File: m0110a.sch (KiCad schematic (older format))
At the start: 177 parts

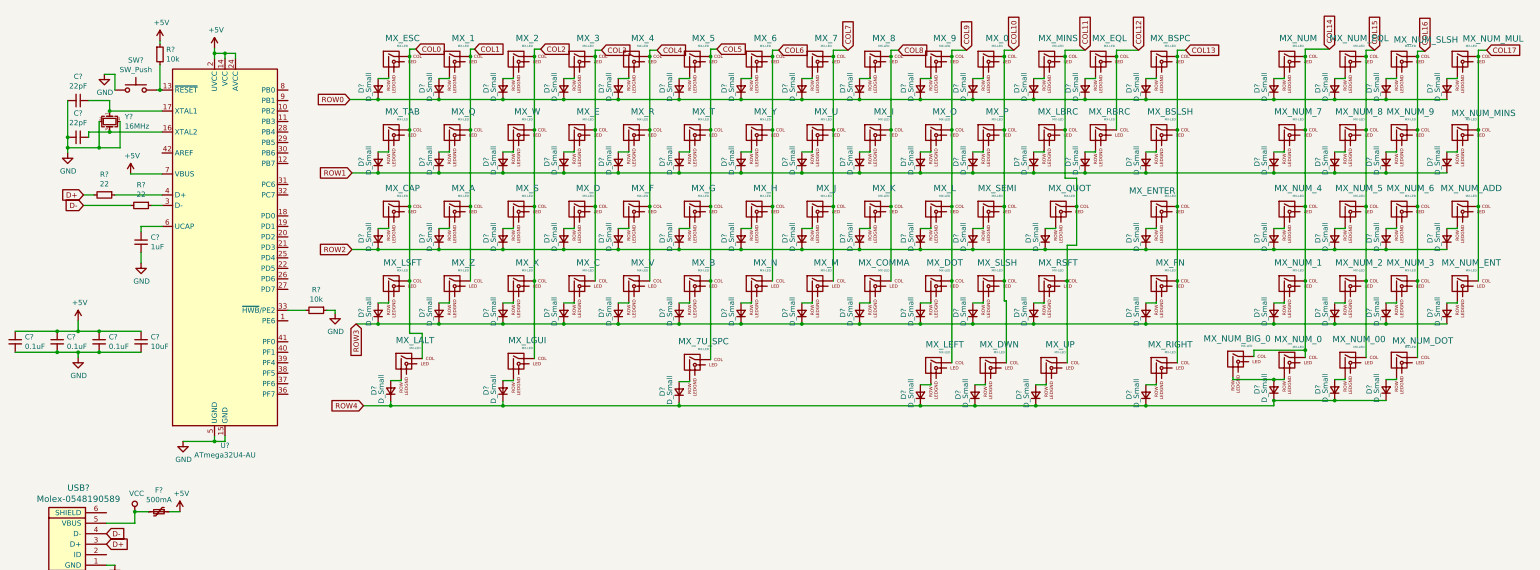
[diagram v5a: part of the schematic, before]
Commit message: Add footprint associations
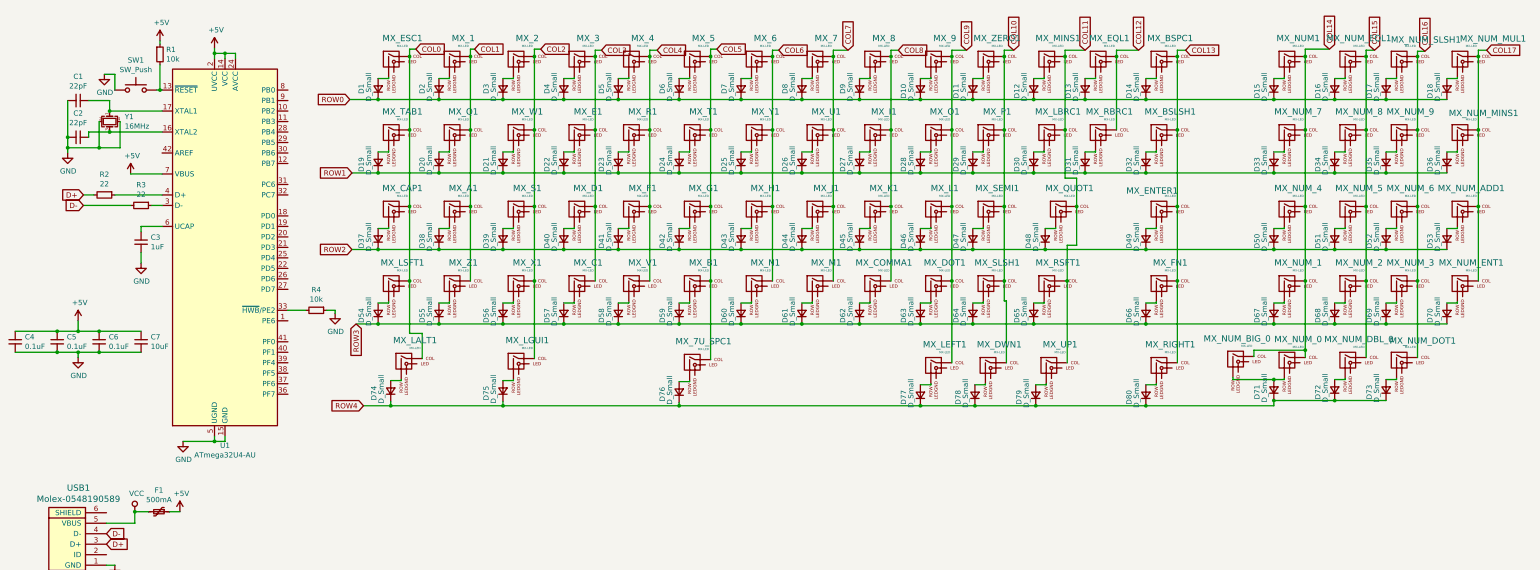
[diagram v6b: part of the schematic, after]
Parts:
- C1, C2, C3, C4, C5, C6, C7: renamed from C?; footprint (none) -> Capacitor_SMD:C_0805_2012Metric
- D1, D10, D11, D12, D13, D14, D15, D16, D17, D18, D19, D2, D20, D21, D22, D23, D24, D25, D26, D27, D28, D29, D3, D30, D31, D32, D33, D34, D35, D36, D37, D38, D39, D4, D40, D41, D42, D43, D44, D45, D46, D47, D48, D49, D5, D50, D51, D52, D53, D54, D55, D56, D57, D58, D59, D6, D60, D61, D62, D63, D64, D65, D66, D67, D68, D69, D7, D70, D71, D72, D73, D74, D75, D76, D77, D78, D79, D8, D80, D9: renamed from D?; footprint (none) -> Diode_SMD:D_SOD-123
- F1: renamed from F?; footprint (none) -> Fuse:Fuse_1206_3216Metric
- MX_1, MX_2, MX_3, MX_4, MX_5, MX_6, MX_7, MX_8, MX_9, MX_NUM_0, MX_NUM_1, MX_NUM_2, MX_NUM_3, MX_NUM_4, MX_NUM_5, MX_NUM_6, MX_NUM_7, MX_NUM_8, MX_NUM_9: footprint (none) -> MX_Alps_Hybrid:MX-1U
- MX_7U_SPC1: renamed from MX_7U_SPC; footprint (none) -> MX_Alps_Hybrid:MX-7U
- MX_A1: renamed from MX_A; footprint (none) -> MX_Alps_Hybrid:MX-1U
- MX_B1: renamed from MX_B; footprint (none) -> MX_Alps_Hybrid:MX-1U
- MX_BSLSH1: renamed from MX_BSLSH; footprint (none) -> MX_Alps_Hybrid:MX-1U
- MX_BSPC1: renamed from MX_BSPC; footprint (none) -> MX_Alps_Hybrid:MX-1.5U
- MX_C1: renamed from MX_C; footprint (none) -> MX_Alps_Hybrid:MX-1U
- MX_CAP1: renamed from MX_CAP; footprint (none) -> MX_Alps_Hybrid:MX-1.75U
- MX_COMMA1: renamed from MX_COMMA; footprint (none) -> MX_Alps_Hybrid:MX-1U
- MX_D1: renamed from MX_D; footprint (none) -> MX_Alps_Hybrid:MX-1U
- MX_DOT1: renamed from MX_DOT; footprint (none) -> MX_Alps_Hybrid:MX-1U
- MX_DWN1: renamed from MX_DWN; footprint (none) -> MX_Alps_Hybrid:MX-1U
- MX_E1: renamed from MX_E; footprint (none) -> MX_Alps_Hybrid:MX-1U
- MX_ENTER1: renamed from MX_ENTER; footprint (none) -> MX_Alps_Hybrid:MX-1.75U
- MX_EQL1: renamed from MX_EQL; footprint (none) -> MX_Alps_Hybrid:MX-1U
- MX_ESC1: renamed from MX_ESC; footprint (none) -> MX_Alps_Hybrid:MX-1U
- MX_F1: renamed from MX_F; footprint (none) -> MX_Alps_Hybrid:MX-1U
- MX_FN1: renamed from MX_FN; footprint (none) -> MX_Alps_Hybrid:MX-1U
- MX_G1: renamed from MX_G; footprint (none) -> MX_Alps_Hybrid:MX-1U
- MX_H1: renamed from MX_H; footprint (none) -> MX_Alps_Hybrid:MX-1U
- MX_I1: renamed from MX_I; footprint (none) -> MX_Alps_Hybrid:MX-1U
- MX_J1: renamed from MX_J; footprint (none) -> MX_Alps_Hybrid:MX-1U
- MX_K1: renamed from MX_K; footprint (none) -> MX_Alps_Hybrid:MX-1U
- MX_L1: renamed from MX_L; footprint (none) -> MX_Alps_Hybrid:MX-1U
- MX_LALT1: renamed from MX_LALT; footprint (none) -> MX_Alps_Hybrid:MX-1.5U
- MX_LBRC1: renamed from MX_LBRC; footprint (none) -> MX_Alps_Hybrid:MX-1U
- MX_LEFT1: renamed from MX_LEFT; footprint (none) -> MX_Alps_Hybrid:MX-1U
- MX_LGUI1: renamed from MX_LGUI; footprint (none) -> MX_Alps_Hybrid:MX-2U
- MX_LSFT1: renamed from MX_LSFT; footprint (none) -> MX_Alps_Hybrid:MX-2.25U
- MX_M1: renamed from MX_M; footprint (none) -> MX_Alps_Hybrid:MX-1U
- MX_MINS1: renamed from MX_MINS; footprint (none) -> MX_Alps_Hybrid:MX-1U
- MX_N1: renamed from MX_N; footprint (none) -> MX_Alps_Hybrid:MX-1U
- MX_NUM1: renamed from MX_NUM; footprint (none) -> MX_Alps_Hybrid:MX-1U
- MX_NUM_ADD1: renamed from MX_NUM_ADD; footprint (none) -> MX_Alps_Hybrid:MX-1U
- MX_NUM_BIG_0: footprint (none) -> MX_Alps_Hybrid:MX-2U
- MX_NUM_DBL_0: renamed from MX_NUM_00; footprint (none) -> MX_Alps_Hybrid:MX-1U
- MX_NUM_DOT1: renamed from MX_NUM_DOT; footprint (none) -> MX_Alps_Hybrid:MX-1U
- MX_NUM_ENT1: renamed from MX_NUM_ENT; footprint (none) -> MX_Alps_Hybrid:MX-2U
- MX_NUM_EQL1: renamed from MX_NUM_EQL; footprint (none) -> MX_Alps_Hybrid:MX-1U
- MX_NUM_MINS1: renamed from MX_NUM_MINS; footprint (none) -> MX_Alps_Hybrid:MX-1U
- MX_NUM_MUL1: renamed from MX_NUM_MUL; footprint (none) -> MX_Alps_Hybrid:MX-1U
- MX_NUM_SLSH1: renamed from MX_NUM_SLSH; footprint (none) -> MX_Alps_Hybrid:MX-1U
- MX_O1: renamed from MX_O; footprint (none) -> MX_Alps_Hybrid:MX-1U
- MX_P1: renamed from MX_P; footprint (none) -> MX_Alps_Hybrid:MX-1U
- MX_Q1: renamed from MX_Q; footprint (none) -> MX_Alps_Hybrid:MX-1U
- MX_QUOT1: renamed from MX_QUOT; footprint (none) -> MX_Alps_Hybrid:MX-1U
- MX_R1: renamed from MX_R; footprint (none) -> MX_Alps_Hybrid:MX-1U
- MX_RBRC1: renamed from MX_RBRC; footprint (none) -> MX_Alps_Hybrid:MX-1U
- MX_RIGHT1: renamed from MX_RIGHT; footprint (none) -> MX_Alps_Hybrid:MX-1U
- MX_RSFT1: renamed from MX_RSFT; footprint (none) -> MX_Alps_Hybrid:MX-1.25U
- MX_S1: renamed from MX_S; footprint (none) -> MX_Alps_Hybrid:MX-1U
- MX_SEMI1: renamed from MX_SEMI; footprint (none) -> MX_Alps_Hybrid:MX-1U
- MX_SLSH1: renamed from MX_SLSH; footprint (none) -> MX_Alps_Hybrid:MX-1U
- MX_T1: renamed from MX_T; footprint (none) -> MX_Alps_Hybrid:MX-1U
- MX_TAB1: renamed from MX_TAB; footprint (none) -> MX_Alps_Hybrid:MX-1.5U
- MX_U1: renamed from MX_U; footprint (none) -> MX_Alps_Hybrid:MX-1U
- MX_UP1: renamed from MX_UP; footprint (none) -> MX_Alps_Hybrid:MX-1U
- MX_V1: renamed from MX_V; footprint (none) -> MX_Alps_Hybrid:MX-1U
- MX_W1: renamed from MX_W; footprint (none) -> MX_Alps_Hybrid:MX-1U
- MX_X1: renamed from MX_X; footprint (none) -> MX_Alps_Hybrid:MX-1U
- MX_Y1: renamed from MX_Y; footprint (none) -> MX_Alps_Hybrid:MX-1U
- MX_Z1: renamed from MX_Z; footprint (none) -> MX_Alps_Hybrid:MX-1U
- MX_ZERO1: renamed from MX_0; footprint (none) -> MX_Alps_Hybrid:MX-1U
- R1, R2, R3, R4: renamed from R?; footprint (none) -> Resistor_SMD:R_0805_2012Metric
- SW1: renamed from SW?; footprint (none) -> random-keyboard-parts:SKQG-1155865
- USB1: renamed from USB?; footprint (none) -> random-keyboard-parts:Molex-0548190589
- Y1: renamed from Y?; footprint (none) -> Crystal:Crystal_SMD_3225-4Pin_3.2x2.5mm
- gave numbers to parts that had none: 1

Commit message: replace symbols with hot swap rgb
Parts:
- removed C1, C2: 22pF, Capacitor_SMD:C_0805_2012Metric, symbol Device:C_Small
- removed C3: 1uF, Capacitor_SMD:C_0805_2012Metric, symbol Device:C_Small
- removed C4, C5, C6: 0.1uF, Capacitor_SMD:C_0805_2012Metric, symbol Device:C_Small
- removed C7: 10uF, Capacitor_SMD:C_0805_2012Metric, symbol Device:C_Small
- removed D1, D10, D11, D12, D13, D14, D15, D16, D17, D18, D19, D2, D20, D21, D22, D23, D24, D25, D26, D27, D28, D29, D3, D30, D31, D32, D33, D34, D35, D36, D37, D38, D39, D4, D40, D41, D42, D43, D44, D45, D46, D47, D48, D49, D5, D50, D51, D52, D53, D54, D55, D56, D57, D58, D59, D6, D60, D61, D62, D63, D64, D65, D66, D67, D68, D69, D7, D70, D71, D72, D73, D74, D75, D76, D77, D78, D79, D8, D80, D9: D_Small, Diode_SMD:D_SOD-123, symbol Device:D_Small
- removed F1: 500mA, Fuse:Fuse_1206_3216Metric, symbol Device:Polyfuse_Small
- removed MX_1, MX_2, MX_3, MX_4, MX_5, MX_6, MX_7, MX_8, MX_9, MX_A1, MX_B1, MX_BSLSH1, MX_C1, MX_COMMA1, MX_D1, MX_DOT1, MX_DWN1, MX_E1, MX_EQL1, MX_ESC1, MX_F1, MX_FN1, MX_G1, MX_H1, MX_I1, MX_J1, MX_K1, MX_L1, MX_LBRC1, MX_LEFT1, MX_M1, MX_MINS1, MX_N1, MX_NUM1, MX_NUM_0, MX_NUM_1, MX_NUM_2, MX_NUM_3, MX_NUM_4, MX_NUM_5, MX_NUM_6, MX_NUM_7, MX_NUM_8, MX_NUM_9, MX_NUM_ADD1, MX_NUM_DBL_0, MX_NUM_DOT1, MX_NUM_EQL1, MX_NUM_MINS1, MX_NUM_MUL1, MX_NUM_SLSH1, MX_O1, MX_P1, MX_Q1, MX_QUOT1, MX_R1, MX_RBRC1, MX_RIGHT1, MX_S1, MX_SEMI1, MX_SLSH1, MX_T1, MX_U1, MX_UP1, MX_V1, MX_W1, MX_X1, MX_Y1, MX_Z1, MX_ZERO1: MX-LED, MX_Alps_Hybrid:MX-1U, symbol MX_Alps_Hybrid:MX-LED
- removed MX_7U_SPC1: MX-LED, MX_Alps_Hybrid:MX-7U, symbol MX_Alps_Hybrid:MX-LED
- removed MX_BSPC1, MX_LALT1, MX_TAB1: MX-LED, MX_Alps_Hybrid:MX-1.5U, symbol MX_Alps_Hybrid:MX-LED
- removed MX_CAP1, MX_ENTER1: MX-LED, MX_Alps_Hybrid:MX-1.75U, symbol MX_Alps_Hybrid:MX-LED
- removed MX_LGUI1, MX_NUM_BIG_0, MX_NUM_ENT1: MX-LED, MX_Alps_Hybrid:MX-2U, symbol MX_Alps_Hybrid:MX-LED
- removed MX_LSFT1: MX-LED, MX_Alps_Hybrid:MX-2.25U, symbol MX_Alps_Hybrid:MX-LED
- removed MX_RSFT1: MX-LED, MX_Alps_Hybrid:MX-1.25U, symbol MX_Alps_Hybrid:MX-LED
- removed R1, R4: 10k, Resistor_SMD:R_0805_2012Metric, symbol Device:R_Small
- removed R2, R3: 22, Resistor_SMD:R_0805_2012Metric, symbol Device:R_Small
- removed SW1: SW_Push, random-keyboard-parts:SKQG-1155865, symbol Switch:SW_Push
- removed U1: ATmega32U4-AU, Package_QFP:TQFP-44_10x10mm_P0.8mm, symbol MCU_Microchip_ATmega:ATmega32U4-AU
- removed USB1: Molex-0548190589, random-keyboard-parts:Molex-0548190589, symbol random-keyboard-parts:Molex-0548190589
- removed Y1: 16MHz, Crystal:Crystal_SMD_3225-4Pin_3.2x2.5mm, symbol Device:Crystal_GND24_Small
- added MX? (x90): CherryMX_LTST-A683CEGBW, symbol CherryMX:CherryMX_LTST-A683CEGBW
- added U?: Teensy++2.0_(C), symbol teensy:Teensy++2.0_(C)

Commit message: connect some of the schematic
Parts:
- removed MX? (x11): CherryMX_LTST-A683CEGBW, symbol CherryMX:CherryMX_LTST-A683CEGBW
- added D? (x78): D_Small, symbol Device:D_Small
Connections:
- net at MX?.2: now also D?.2 (A) (x53)
- new net: D?.1 (K), D?.1 (K), D?.1 (K), D?.1 (K), D?.1 (K), D?.1 (K), D?.1 (K), D?.1 (K), D?.1 (K), D?.1 (K), D?.1 (K), D?.1 (K), D?.1 (K), D?.1 (K), D?.1 (K), D?.1 (K), D?.1 (K), D?.1 (K) (x2)
- new net: D?.1 (K), D?.1 (K), D?.1 (K), D?.1 (K), D?.1 (K), D?.1 (K), D?.1 (K), D?.1 (K), D?.1 (K), D?.1 (K), D?.1 (K), D?.1 (K), D?.1 (K), D?.1 (K), D?.1 (K), D?.1 (K), D?.1 (K)
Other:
- moved on the sheet: MX?
